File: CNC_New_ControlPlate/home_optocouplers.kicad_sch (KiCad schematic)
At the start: 25 parts, among them U1 PC847

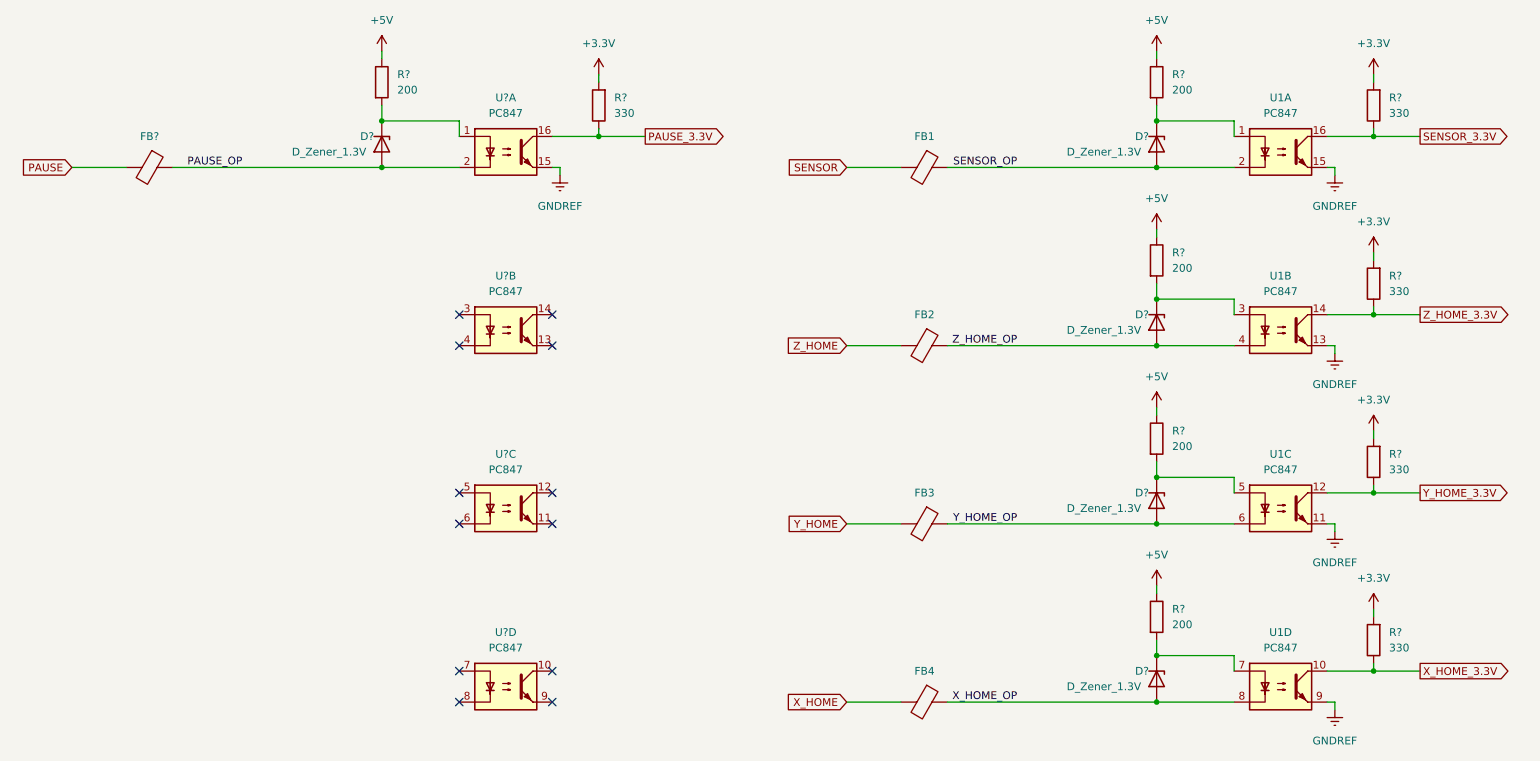
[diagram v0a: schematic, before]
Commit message: [*] Исправлены ошибки с выходами питания. [+] Добавлены обозначения элементов
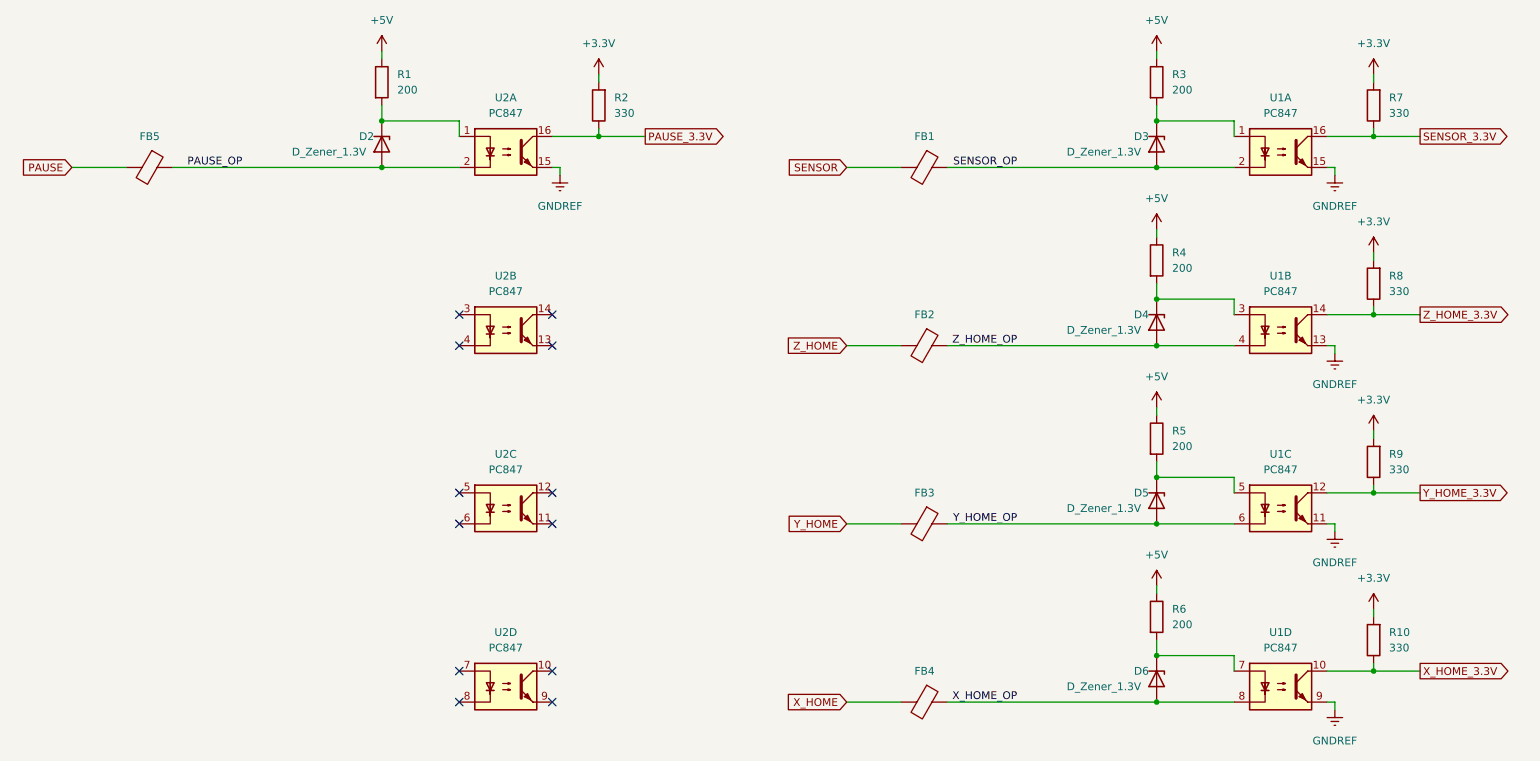
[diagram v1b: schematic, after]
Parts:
- gave numbers to parts that had none: 17

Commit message: Edit footprints
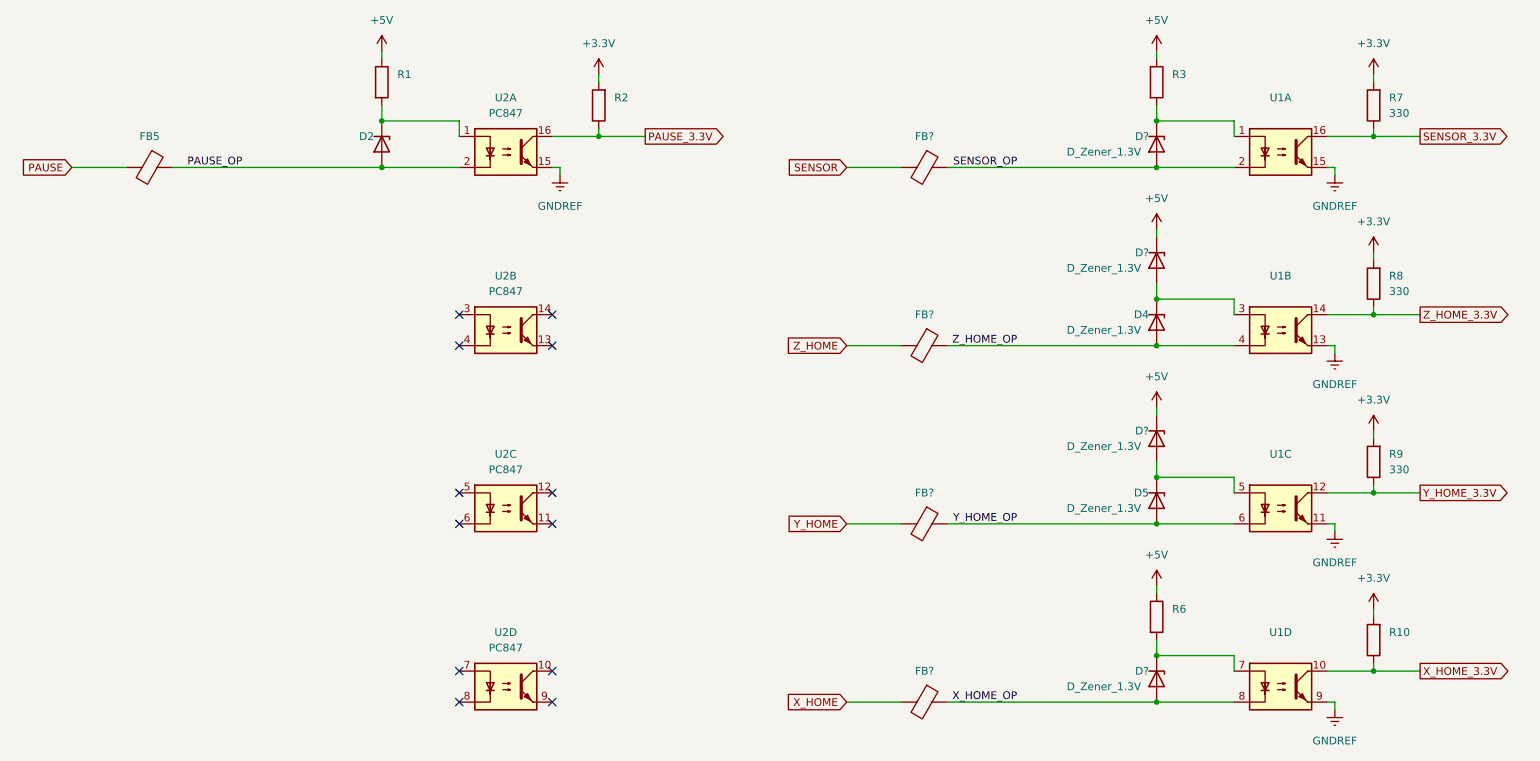
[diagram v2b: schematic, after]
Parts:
- removed D3, D6: D_Zener_1.3V, Diode_SMD:D_0603_1608Metric, symbol Device:D_Zener
- removed FB1, FB2, FB3, FB4: FerriteBead, Resistor_SMD:R_0603_1608Metric, symbol Device:FerriteBead
- removed R4, R5: 200, Resistor_SMD:R_0603_1608Metric, symbol Device:R
- added D? (x4): D_Zener_1.3V, Diode_THT:D_A-405_P7.62mm_Horizontal, symbol Device:D_Zener
- added FB? (x4): FerriteBead, Resistor_THT:R_Axial_DIN0207_L6.3mm_D2.5mm_P7.62mm_Horizontal, symbol Device:FerriteBead
- D2: value D_Zener_1.3V -> (none); footprint Diode_SMD:D_0603_1608Metric -> (none)
- FB5: value FerriteBead -> (none); footprint Resistor_SMD:R_0603_1608Metric -> (none)
- R1, R3, R6: value 200 -> (none); footprint Resistor_SMD:R_0603_1608Metric -> (none)
- R10, R2: value 330 -> (none); footprint Resistor_SMD:R_0603_1608Metric -> (none)
- U1: value PC847 -> (none); footprint Package_DIP:DIP-16_W7.62mm_Socket_LongPads -> (none)
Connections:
- net +5V: now also D?.1 (K), D?.1 (K)
- net SENSOR: now also FB?.2
- net SENSOR_OP: now also D?.2 (A), FB?.1
- net X_HOME: now also FB?.2
- net X_HOME_OP: now also D?.2 (A), FB?.1
- net Y_HOME: now also FB?.2
- net Y_HOME_OP: now also FB?.1
- net Z_HOME: now also FB?.2
- net Z_HOME_OP: now also FB?.1
- net at D5.1 (K), U1.5: now also D?.2 (A)
- net at D4.1 (K), U1.3: now also D?.2 (A)
- net at R3.2, U1.1: now also D?.1 (K)
- net at R6.2, U1.7: now also D?.1 (K)

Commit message: [*] Разводка платы в один слой (осталось 7 перемычек)
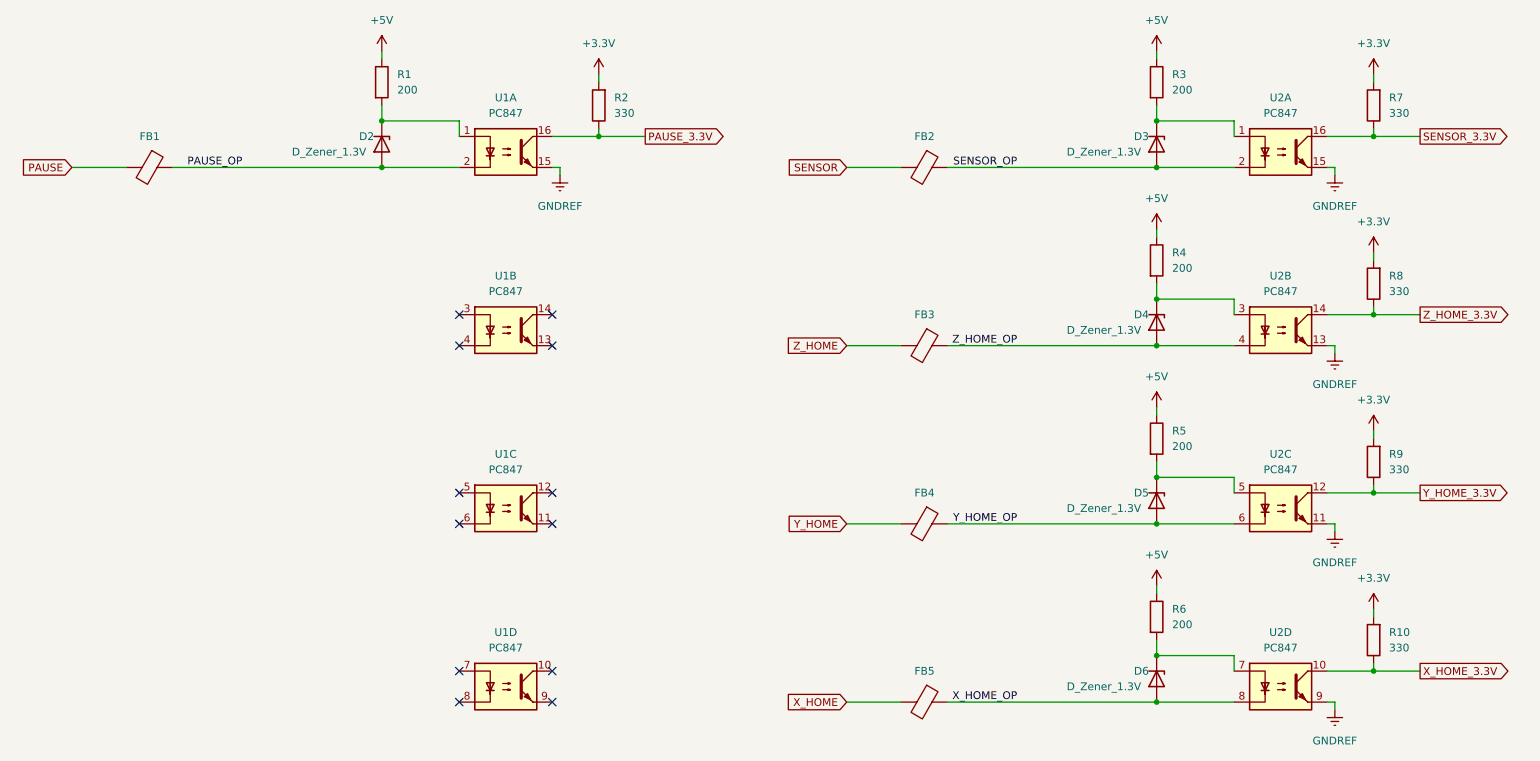
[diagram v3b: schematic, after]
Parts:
- removed D4, D5: D_Zener_1.3V, Diode_SMD:D_0603_1608Metric, symbol Device:D_Zener
- added R4, R5: 200, Resistor_SMD:R_0603_1608Metric, symbol Device:R
- D2: value (none) -> D_Zener_1.3V; footprint (none) -> Diode_THT:D_A-405_P7.62mm_Horizontal
- FB1: renamed from FB5; value (none) -> FerriteBead; footprint (none) -> Resistor_THT:R_Axial_DIN0207_L6.3mm_D2.5mm_P7.62mm_Horizontal
- R1, R3, R6: value (none) -> 200; footprint (none) -> Resistor_SMD:R_0603_1608Metric
- R10, R2: value (none) -> 330; footprint (none) -> Resistor_SMD:R_0603_1608Metric
- U2: renamed from U1; value (none) -> PC847; footprint (none) -> Package_DIP:DIP-16_W7.62mm_Socket_LongPads
- gave numbers to parts that had none: 8
- renumbered U2 to U1
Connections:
- net +5V: now also R4.1, R5.1; no longer D4.1 (K), D5.1 (K)
- net Y_HOME_OP: now also D5.2 (A)
- net Z_HOME_OP: now also D4.2 (A)
- net at U2.5: now also D5.1 (K), R5.2; no longer D5.2 (A)
- net at U2.3: now also D4.1 (K), R4.2; no longer D4.2 (A)
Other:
- moved on the sheet: D4, D5

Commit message: [*] Разведена плата в один слой (3 перемычки на шине 5В; 2 соединения земли через плату STM
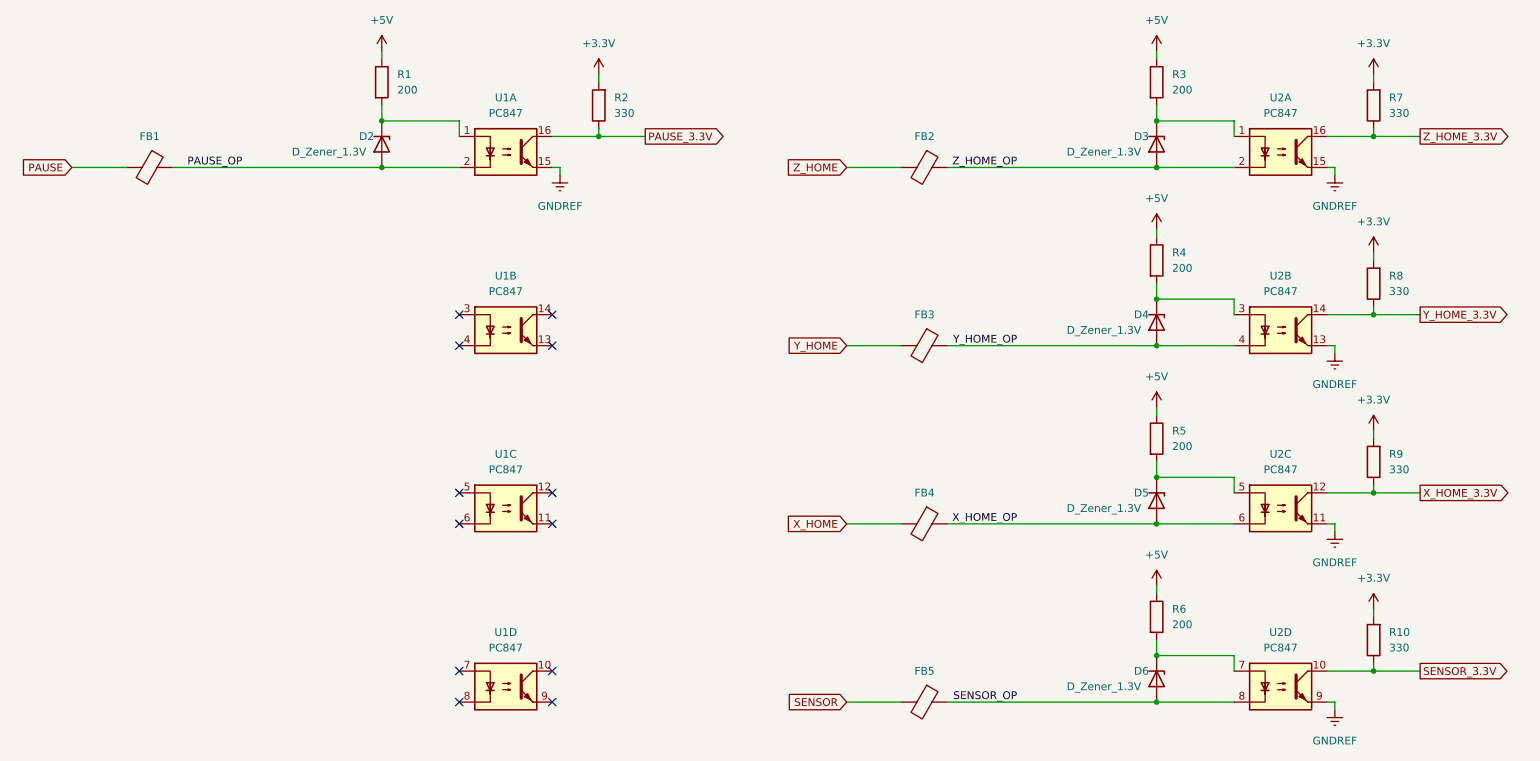
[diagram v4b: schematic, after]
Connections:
- net SENSOR: now also FB5.2; no longer FB2.2
- net SENSOR_3.3V: now also R10.1, U2.10; no longer R7.1, U2.16
- net SENSOR_OP: now also D6.2 (A), FB5.1, U2.8; no longer D3.2 (A), FB2.1, U2.2
- net X_HOME: now also FB4.2; no longer FB5.2
- net X_HOME_3.3V: now also R9.1, U2.12; no longer R10.1, U2.10
- net X_HOME_OP: now also D5.2 (A), FB4.1, U2.6; no longer D6.2 (A), FB5.1, U2.8
- net Y_HOME: now also FB3.2; no longer FB4.2
- net Y_HOME_3.3V: now also R8.1, U2.14; no longer R9.1, U2.12
- net Y_HOME_OP: now also D4.2 (A), FB3.1, U2.4; no longer D5.2 (A), FB4.1, U2.6
- net Z_HOME: now also FB2.2; no longer FB3.2
- net Z_HOME_3.3V: now also R7.1, U2.16; no longer R8.1, U2.14
- net Z_HOME_OP: now also D3.2 (A), FB2.1, U2.2; no longer D4.2 (A), FB3.1, U2.4
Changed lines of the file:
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@@
     (stroke (width 0) (type default) (color 0 0 0 0))
   )
-  (label "Y_HOME_OP" (at 182.88 110.49 180)
+  (label "Y_HOME_OP" (at 182.88 81.28 180)
     (effects (font (size 1.27 1.27)) (justify right bottom))
   )
-  (label "X_HOME_OP" (at 182.88 139.7 180)
+  (label "X_HOME_OP" (at 182.88 110.49 180)
     (effects (font (size 1.27 1.27)) (justify right bottom))
   )
-  (label "Z_HOME_OP" (at 182.88 81.28 180)
+  (label "Z_HOME_OP" (at 182.88 52.07 180)
     (effects (font (size 1.27 1.27)) (justify right bottom))
   )
@@
     (effects (font (size 1.27 1.27)) (justify right bottom))
   )
-  (label "SENSOR_OP" (at 182.88 52.07 180)
+  (label "SENSOR_OP" (at 182.88 139.7 180)
     (effects (font (size 1.27 1.27)) (justify right bottom))
   )
@@
     )
   )
-  (global_label "Z_HOME_3.3V" (shape output) (at 248.92 76.2 0) (fields_autoplaced)
+  (global_label "Z_HOME_3.3V" (shape output) (at 248.92 46.99 0) (fields_autoplaced)
     (effects (font (size 1.27 1.27)) (justify left))
-    (property "Intersheet References" "${INTERSHEET_REFS}" (id 0) (at 263.8517 76.1206 0)
+    (property "Intersheet References" "${INTERSHEET_REFS}" (id 0) (at 263.8517 46.9106 0)
       (effects (font (size 1.27 1.27)) (justify left) hide)
     )
   )
-  (global_label "Y_HOME" (shape input) (at 154.94 110.49 180) (fields_autoplaced)
+  (global_label "Y_HOME" (shape input) (at 154.94 81.28 180) (fields_autoplaced)
     (effects (font (size 1.27 1.27)) (justify right))
-    (property "Intersheet References" "${INTERSHEET_REFS}" (id 0) (at 145.2093 110.4106 0)
+    (property "Intersheet References" "${INTERSHEET_REFS}" (id 0) (at 145.2093 81.2006 0)
       (effects (font (size 1.27 1.27)) (justify right) hide)
     )
   )
-  (global_label "X_HOME" (shape input) (at 154.94 139.7 180) (fields_autoplaced)
+  (global_label "X_HOME" (shape input) (at 154.94 110.49 180) (fields_autoplaced)
     (effects (font (size 1.27 1.27)) (justify right))
-    (property "Intersheet References" "${INTERSHEET_REFS}" (id 0) (at 145.0883 139.6206 0)
+    (property "Intersheet References" "${INTERSHEET_REFS}" (id 0) (at 145.0883 110.4106 0)
       (effects (font (size 1.27 1.27)) (justify right) hide)
     )
@@
     )
   )
-  (global_label "SENSOR_3.3V" (shape output) (at 248.92 46.99 0) (fields_autoplaced)
+  (global_label "SENSOR_3.3V" (shape output) (at 248.92 134.62 0) (fields_autoplaced)
     (effects (font (size 1.27 1.27)) (justify left))
-    (property "Intersheet References" "${INTERSHEET_REFS}" (id 0) (at 263.9121 46.9106 0)
+    (property "Intersheet References" "${INTERSHEET_REFS}" (id 0) (at 263.9121 134.5406 0)
       (effects (font (size 1.27 1.27)) (justify left) hide)
     )
   )
-  (global_label "Z_HOME" (shape input) (at 154.94 81.28 180) (fields_autoplaced)
+  (global_label "Z_HOME" (shape input) (at 154.94 52.07 180) (fields_autoplaced)
     (effects (font (size 1.27 1.27)) (justify right))
-    (property "Intersheet References" "${INTERSHEET_REFS}" (id 0) (at 145.0883 81.2006 0)
+    (property "Intersheet References" "${INTERSHEET_REFS}" (id 0) (at 145.0883 51.9906 0)
       (effects (font (size 1.27 1.27)) (justify right) hide)
     )
   )
-  (global_label "Y_HOME_3.3V" (shape output) (at 248.92 105.41 0) (fields_autoplaced)
+  (global_label "Y_HOME_3.3V" (shape output) (at 248.92 76.2 0) (fields_autoplaced)
     (effects (font (size 1.27 1.27)) (justify left))
-    (property "Intersheet References" "${INTERSHEET_REFS}" (id 0) (at 263.7307 105.3306 0)
+    (property "Intersheet References" "${INTERSHEET_REFS}" (id 0) (at 263.7307 76.1206 0)
       (effects (font (size 1.27 1.27)) (justify left) hide)
     )
   )
-  (global_label "X_HOME_3.3V" (shape output) (at 248.92 134.62 0) (fields_autoplaced)
+  (global_label "X_HOME_3.3V" (shape output) (at 248.92 105.41 0) (fields_autoplaced)
     (effects (font (size 1.27 1.27)) (justify left))
-    (property "Intersheet References" "${INTERSHEET_REFS}" (id 0) (at 263.8517 134.5406 0)
+    (property "Intersheet References" "${INTERSHEET_REFS}" (id 0) (at 263.8517 105.3306 0)
       (effects (font (size 1.27 1.27)) (justify left) hide)
     )
   )
-  (global_label "SENSOR" (shape input) (at 154.94 52.07 180) (fields_autoplaced)
+  (global_label "SENSOR" (shape input) (at 154.94 139.7 180) (fields_autoplaced)
     (effects (font (size 1.27 1.27)) (justify right))
-    (property "Intersheet References" "${INTERSHEET_REFS}" (id 0) (at 145.0279 51.9906 0)
+    (property "Intersheet References" "${INTERSHEET_REFS}" (id 0) (at 145.0279 139.6206 0)
       (effects (font (size 1.27 1.27)) (justify right) hide)
     )
